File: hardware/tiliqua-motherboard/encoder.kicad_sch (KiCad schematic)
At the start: 10 parts, among them SW3 RotaryEncoder_Switch

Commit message: add some part numbers
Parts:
- R13, R14, R21, R22, R29, R30: lcsc# C60490 -> C25744
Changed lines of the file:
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@@
 			)
 		)
-		(property "lcsc#" "C60490"
+		(property "lcsc#" "C25744"
+			(at 144.78 86.36 0)
+			(effects
+				(font
+					(size 1.27 1.27)
+				)
+				(hide yes)
+			)
+		)
+		(property "Tol" ""
 			(at 144.78 86.36 0)
 			(effects
@@
 			)
 		)
-		(property "lcsc#" "C60490"
+		(property "lcsc#" "C25744"
+			(at 143.51 67.31 0)
+			(effects
+				(font
+					(size 1.27 1.27)
+				)
+				(hide yes)
+			)
+		)
+		(property "Tol" ""
 			(at 143.51 67.31 0)
 			(effects
@@
 			)
 		)
+		(property "Tol" ""
+			(at 161.29 90.17 0)
+			(effects
+				(font
+					(size 1.27 1.27)
+				)
+				(hide yes)
+			)
+		)
 		(pin "1"
 		)
@@
 			)
 		)
-		(property "lcsc#" "C60490"
+		(property "lcsc#" "C25744"
+			(at 132.08 78.74 0)
+			(effects
+				(font
+					(size 1.27 1.27)
+				)
+				(hide yes)
+			)
+		)
+		(property "Tol" ""
 			(at 132.08 78.74 0)
 			(effects
@@
 			)
 		)
-		(property "lcsc#" "C60490"
+		(property "lcsc#" "C25744"
+			(at 137.16 78.74 0)
+			(effects
+				(font
+					(size 1.27 1.27)
+				)
+				(hide yes)
+			)
+		)
+		(property "Tol" ""
 			(at 137.16 78.74 0)
 			(effects
@@
 			)
 		)
-		(property "lcsc#" "C60490"
+		(property "lcsc#" "C25744"
+			(at 144.78 83.82 0)
+			(effects
+				(font
+					(size 1.27 1.27)
+				)
+				(hide yes)
+			)
+		)
+		(property "Tol" ""
 			(at 144.78 83.82 0)
 			(effects
@@
 			)
 		)
+		(property "Tol" ""
+			(at 151.13 72.39 0)
+			(effects
+				(font
+					(size 1.27 1.27)
+				)
+				(hide yes)
+			)
+		)
 		(pin "1"
 		)
@@
 			)
 		)
+		(property "Tol" ""
+			(at 151.13 90.17 0)
+			(effects
+				(font
+					(size 1.27 1.27)
+				)
+				(hide yes)
+			)
+		)
 		(pin "1"
 		)
@@
 			)
 		)
+		(property "Tol" ""
+			(at 120.65 76.2 0)
+			(effects
+				(font
+					(size 1.27 1.27)
+				)
+				(hide yes)
+			)
+		)
 		(pin "S2"
 		)
@@
 			)
 		)
-		(property "lcsc#" "C60490"
+		(property "lcsc#" "C25744"
 			(at 123.19 62.23 0)
 			(effects
+				(font
+					(size 1.27 1.27)
+				)
+				(hide yes)
+			)
+		)
+		(property "Tol" ""
+			(at 123.19 62.23 0)
+			(effects

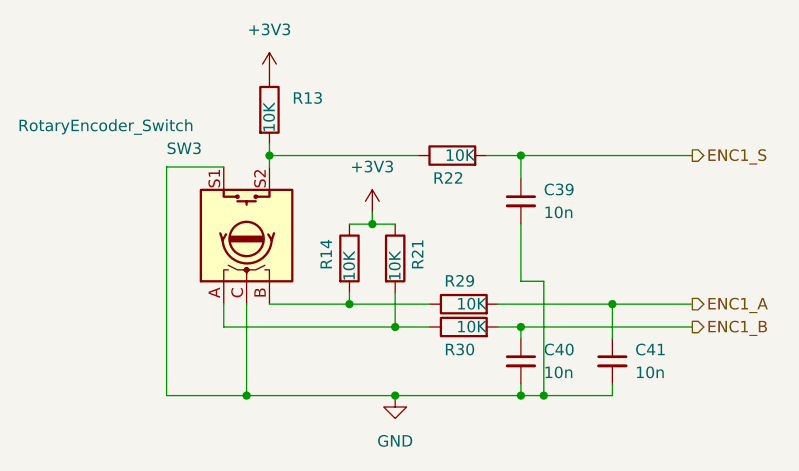
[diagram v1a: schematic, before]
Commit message: hw/mobo-r3: assign remaining part numbers
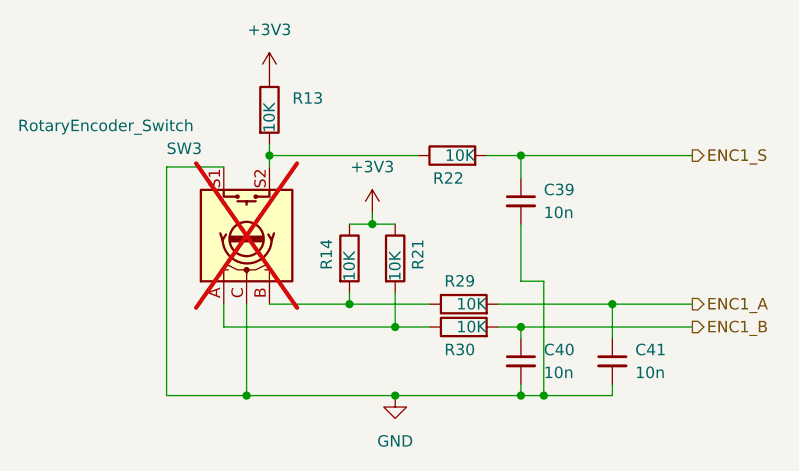
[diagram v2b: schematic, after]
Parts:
- SW3: now not fitted
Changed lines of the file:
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@@
 		(in_bom yes)
 		(on_board yes)
-		(dnp no)
+		(dnp yes)
 		(property "Reference" "SW3"
 			(at 111.76 66.548 90)

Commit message: hw/mobo-r3: add LCSC database / associations
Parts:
- C39, C40, C41: LCSC (none) -> C15195
- R13, R14, R21, R22, R29, R30: LCSC (none) -> C25744
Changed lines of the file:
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@@
+			)
+		)
+		(property "LCSC" "C25744"
+			(at 146.05 88.9 0)
+			(effects
+				(font
+					(size 1.27 1.27)
+				)
+				(hide yes)
 			)
 		)
@@
 		(property "Tol" ""
 			(at 143.51 67.31 0)
+			(effects
+				(font
+					(size 1.27 1.27)
+				)
+				(hide yes)
+			)
+		)
+		(property "LCSC" "C25744"
+			(at 144.78 69.85 0)
 			(effects
 				(font
@@
 			)
 		)
+		(property "LCSC" "C15195"
+			(at 163.83 88.9063 0)
+			(effects
+				(font
+					(size 1.27 1.27)
+				)
+				(hide yes)
+			)
+		)
 		(pin "1"
 		)
@@
 			)
 		)
+		(property "LCSC" "C25744"
+			(at 129.54 80.01 0)
+			(effects
+				(font
+					(size 1.27 1.27)
+				)
+				(hide yes)
+			)
+		)
 		(pin "1"
 		)
@@
 		(property "Tol" ""
 			(at 137.16 78.74 0)
+			(effects
+				(font
+					(size 1.27 1.27)
+				)
+				(hide yes)
+			)
+		)
+		(property "LCSC" "C25744"
+			(at 139.7 80.01 0)
 			(effects
 				(font
@@
 			)
 		)
+		(property "LCSC" "C25744"
+			(at 146.05 81.28 0)
+			(effects
+				(font
+					(size 1.27 1.27)
+				)
+				(hide yes)
+			)
+		)
 		(pin "1"
 		)
@@
 			)
 		)
+		(property "LCSC" "C15195"
+			(at 153.67 71.1263 0)
+			(effects
+				(font
+					(size 1.27 1.27)
+				)
+				(hide yes)
+			)
+		)
 		(pin "1"
 		)
@@
 			)
 		)
+		(property "LCSC" "C15195"
+			(at 153.67 88.9063 0)
+			(effects
+				(font
+					(size 1.27 1.27)
+				)
+				(hide yes)
+			)
+		)
 		(pin "1"
 		)
@@
 			(effects
 				(font
+					(size 1.27 1.27)
+				)
+				(hide yes)
+			)
+		)
+		(property "LCSC" "C25744"
+			(at 125.73 60.96 0)
+			(effects
+				(font
